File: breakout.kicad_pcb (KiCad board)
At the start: 2 copper layers, 32 parts, among them CON1 SD_Card, CON2 USB-MICRO-AB, P2 CONN_01X40, P3 CONN_01X40, P4 CONN_01X40, P5 A-DF-09-A/KG-T4S, SW1 SW_PUSH

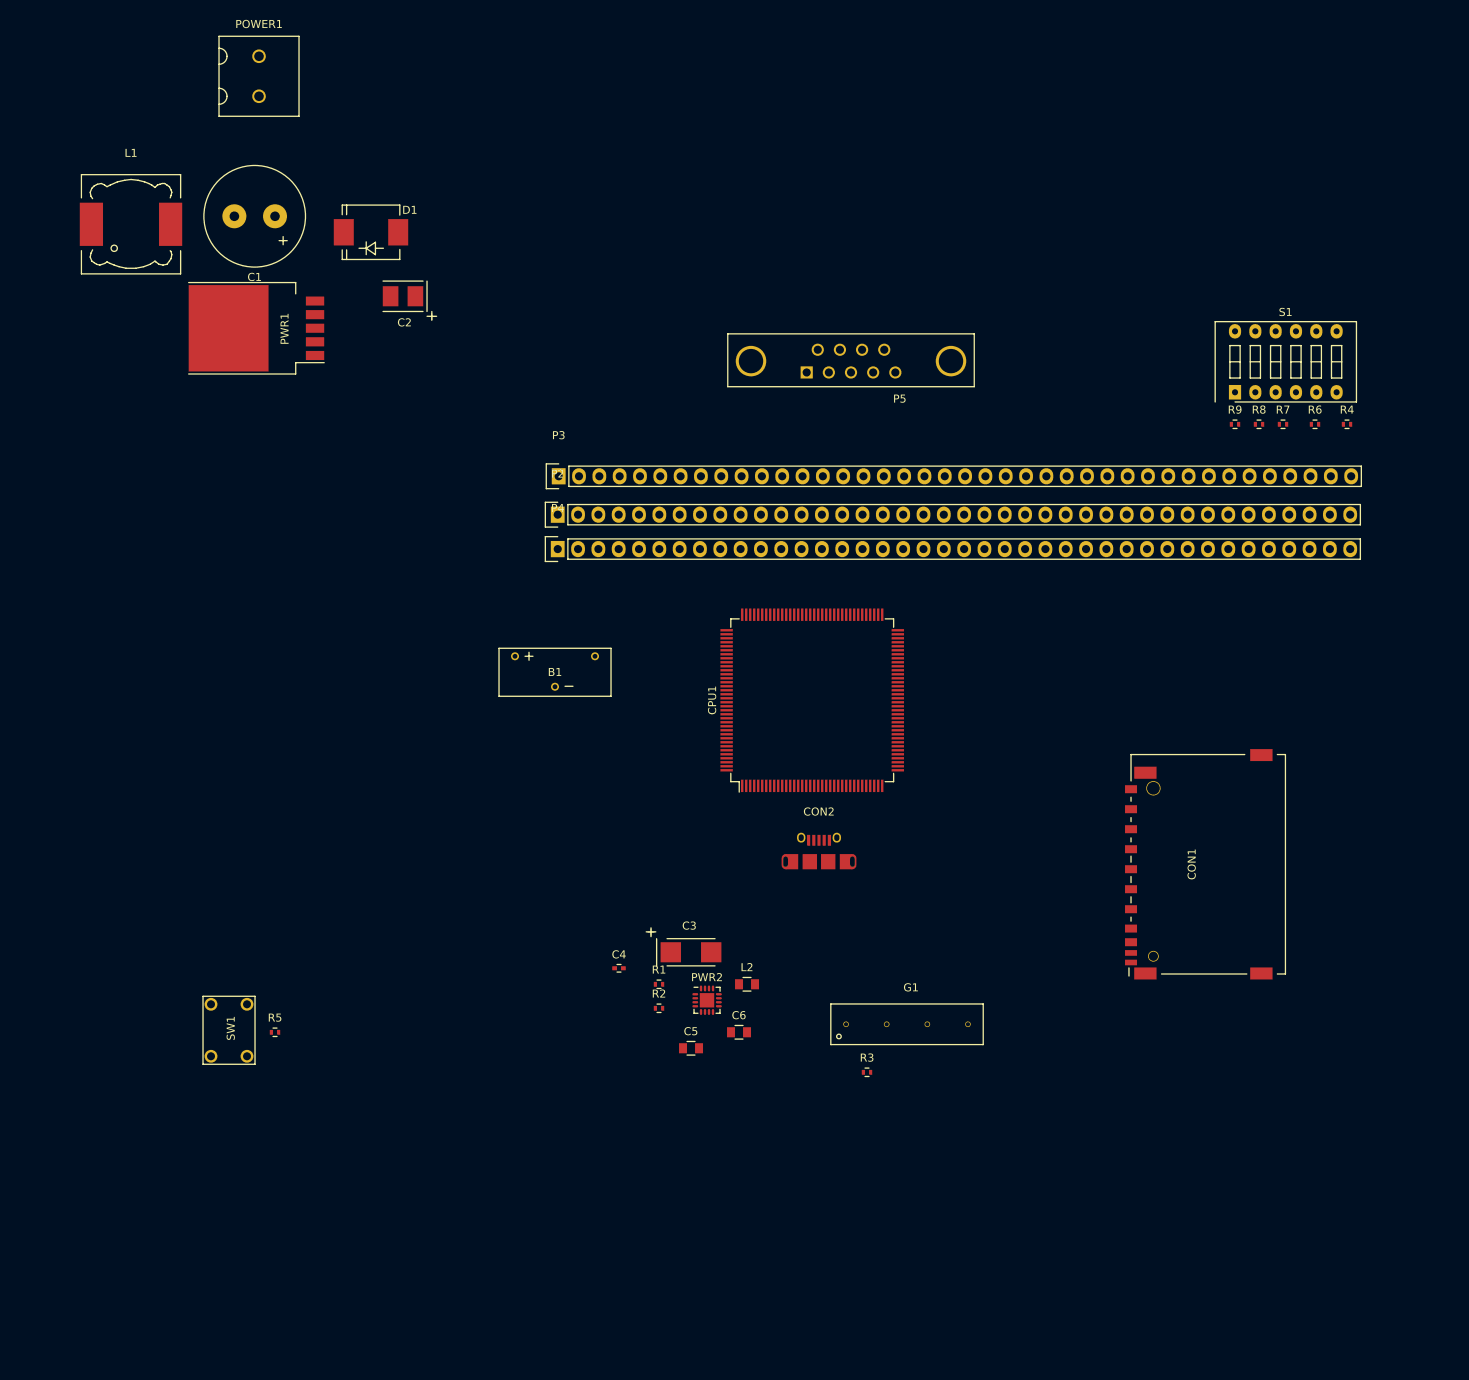
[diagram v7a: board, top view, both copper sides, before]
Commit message: added more nets
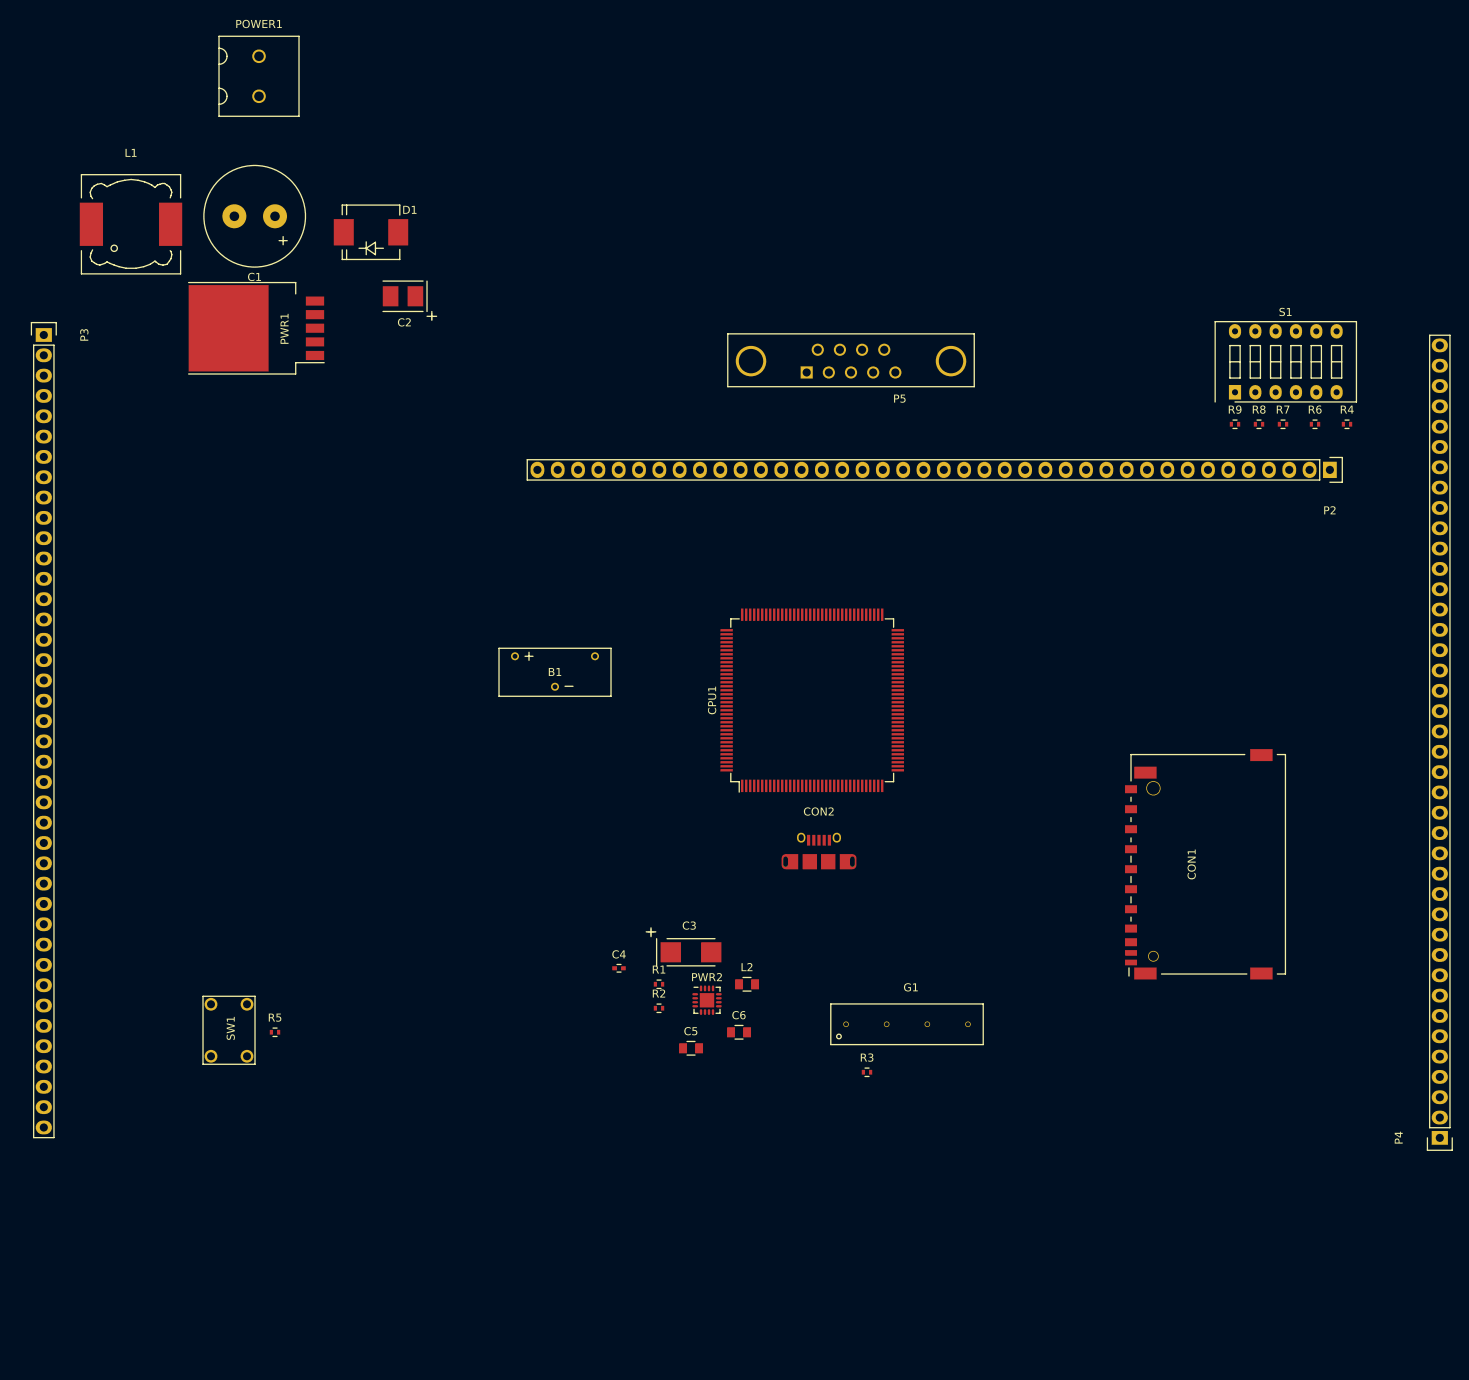
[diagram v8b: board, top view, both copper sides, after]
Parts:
- moved P4 132.6 mm to (194.6, 235.2), turned to 90 degrees
- moved P2 96.7 mm to (180.9, 151.7), turned to 180 degrees
- moved P3 66.7 mm to (20.1, 134.8), turned to 270 degrees
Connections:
- net Net-(CON2-Pad2) renamed /USB0_D-
- net Net-(CON2-Pad3) renamed /USB0_D+
- net Net-(CON2-Pad4) renamed /USB0_ID
- CPU1 pad 100: (no net) -> /P6_10
- CPU1 pad 101: (no net) -> /P6_11
- CPU1 pad 103: (no net) -> /P6_12
- CPU1 pad 104: (no net) -> /P2_10
- CPU1 pad 105: (no net) -> /P2_11
- CPU1 pad 106: (no net) -> /P2_12
- CPU1 pad 108: (no net) -> /P2_13
- CPU1 pad 110: (no net) -> /P7_0
- CPU1 pad 112: (no net) -> /P3_0
- CPU1 pad 113: (no net) -> /P7_1
- CPU1 pad 114: (no net) -> /P3_1
- CPU1 pad 115: (no net) -> /P7_2
- CPU1 pad 116: (no net) -> /P3_2
- CPU1 pad 117: (no net) -> /P7_3
- CPU1 pad 118: (no net) -> /SPI_SCK
- CPU1 pad 119: (no net) -> /P3_4
- CPU1 pad 120: (no net) -> /PF_4
- CPU1 pad 121: (no net) -> /P3_5
- CPU1 pad 122: (no net) -> /SPI_MISO
- CPU1 pad 123: (no net) -> /SPI_MOSI
- CPU1 pad 124: (no net) -> /SPI_SSEL
- CPU1 pad 125: (no net) -> /RTCX1
- CPU1 pad 126: (no net) -> /RTCX2
- CPU1 pad 129: (no net) -> /RTC_ALARM
- CPU1 pad 130: (no net) -> /WAKEUP0
- CPU1 pad 132: (no net) -> /P7_4
- CPU1 pad 133: (no net) -> /P7_5
- CPU1 pad 134: (no net) -> /P7_6
- CPU1 pad 136: (no net) -> /ADC0_7
- CPU1 pad 138: (no net) -> /ADC0_4
- CPU1 pad 139: (no net) -> /ADC0_3
- CPU1 pad 140: (no net) -> /P7_7
- CPU1 pad 142: (no net) -> /ADC0_6
- CPU1 pad 143: (no net) -> /ADC0_2
- CPU1 pad 144: (no net) -> /ADC0_5
- CPU1 pad 73: (no net) -> /P6_0
- CPU1 pad 74: (no net) -> /P6_1
- CPU1 pad 78: (no net) -> /P6_2
- CPU1 pad 79: (no net) -> /P6_3
- CPU1 pad 80: (no net) -> /P6_4
- CPU1 pad 82: (no net) -> /P6_5
- CPU1 pad 83: (no net) -> /P6_6
- CPU1 pad 84: (no net) -> /P2_2
- CPU1 pad 85: (no net) -> /P6_7
- CPU1 pad 86: (no net) -> /P6_8
- CPU1 pad 88: (no net) -> /P2_4
- CPU1 pad 89: (no net) -> /USB1_D+
- CPU1 pad 90: (no net) -> /USB1_D-
- CPU1 pad 91: (no net) -> /P2_5
- CPU1 pad 92: (no net) -> /I2C0_SCL
- CPU1 pad 93: (no net) -> /I2C0_SDA
- CPU1 pad 95: (no net) -> /P2_6
- CPU1 pad 97: (no net) -> /P6_9
- CPU1 pad 99: (no net) -> /CLK2
- P2 pad 25: (no net) -> /P6_0
- P2 pad 26: (no net) -> /P6_1
- P2 pad 27: (no net) -> /P6_2
- P2 pad 28: (no net) -> /P6_3
- P2 pad 29: (no net) -> /P6_4
- P2 pad 30: (no net) -> /P6_5
- P2 pad 31: (no net) -> /P6_6
- P2 pad 32: (no net) -> /P2_2
- P2 pad 33: (no net) -> /P6_7
- P2 pad 34: (no net) -> /P6_8
- P2 pad 35: (no net) -> /P2_4
- P2 pad 36: (no net) -> /USB1_D+
- P2 pad 37: (no net) -> /USB1_D-
- P2 pad 38: (no net) -> /P2_5
- P2 pad 39: (no net) -> /I2C0_SCL
- P2 pad 40: (no net) -> /I2C0_SDA
- P3 pad 1: (no net) -> /P2_6
- P3 pad 10: (no net) -> /P2_11
- P3 pad 11: (no net) -> /P2_12
- P3 pad 12: (no net) -> /P2_13
- P3 pad 13: (no net) -> /P7_0
- P3 pad 14: (no net) -> /P3_0
- P3 pad 15: (no net) -> /P7_1
- P3 pad 16: (no net) -> /P3_1
- P3 pad 17: (no net) -> /P7_2
- P3 pad 18: (no net) -> /P3_2
- P3 pad 19: (no net) -> /P7_3
- P3 pad 2: (no net) -> /P6_9
- P3 pad 20: (no net) -> /SPI_SCK
- P3 pad 21: (no net) -> /P3_4
- P3 pad 22: (no net) -> /PF_4
- P3 pad 23: (no net) -> /P3_5
- P3 pad 24: (no net) -> /SPI_MISO
- P3 pad 25: (no net) -> /SPI_MOSI
- P3 pad 26: (no net) -> /SPI_SSEL
- P3 pad 27: (no net) -> /RTCX1
- P3 pad 28: (no net) -> /RTCX2
- P3 pad 29: (no net) -> /RTC_ALARM
- P3 pad 3: (no net) -> /P2_8
- P3 pad 30: (no net) -> /WAKEUP0
- P3 pad 31: (no net) -> /P7_4
- P3 pad 32: (no net) -> /P7_5
- P3 pad 33: (no net) -> /P7_6
- P3 pad 34: (no net) -> /ADC0_7
- P3 pad 35: (no net) -> /ADC0_4
- P3 pad 36: (no net) -> /ADC0_3
- P3 pad 37: (no net) -> /P7_7
- P3 pad 38: (no net) -> /ADC0_6
- P3 pad 39: (no net) -> /ADC0_2
- P3 pad 4: (no net) -> /CLK2
- P3 pad 40: (no net) -> /ADC0_5
- P3 pad 5: (no net) -> /P6_10
- P3 pad 6: (no net) -> /P6_11
- P3 pad 7: (no net) -> /P2_9
- P3 pad 8: (no net) -> /P6_12
- P3 pad 9: (no net) -> /P2_10
- PWR2 pad 13: /VSW -> (no net)
- PWR2 pad 14: GND -> (no net)
- PWR2 pad 15: GND -> (no net)
- PWR2 pad 16: /VSW -> (no net)
- PWR2 pad 17: GND -> Net-(PWR2-Pad17)
